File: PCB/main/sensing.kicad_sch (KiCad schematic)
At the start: 2 parts

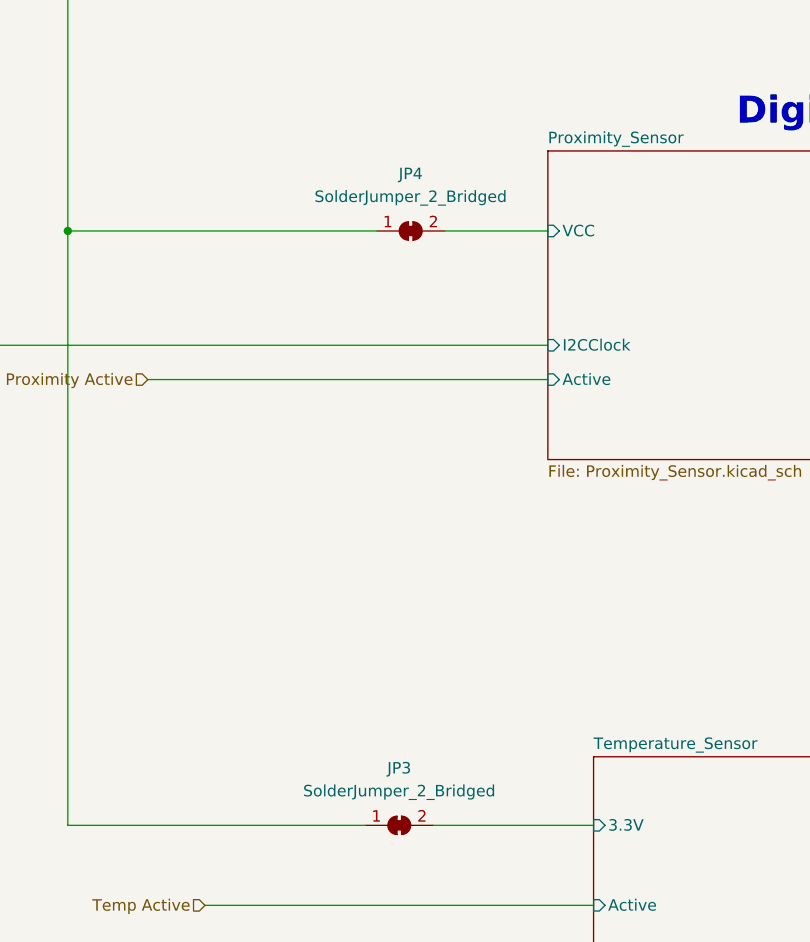
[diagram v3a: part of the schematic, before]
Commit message: Add footprints
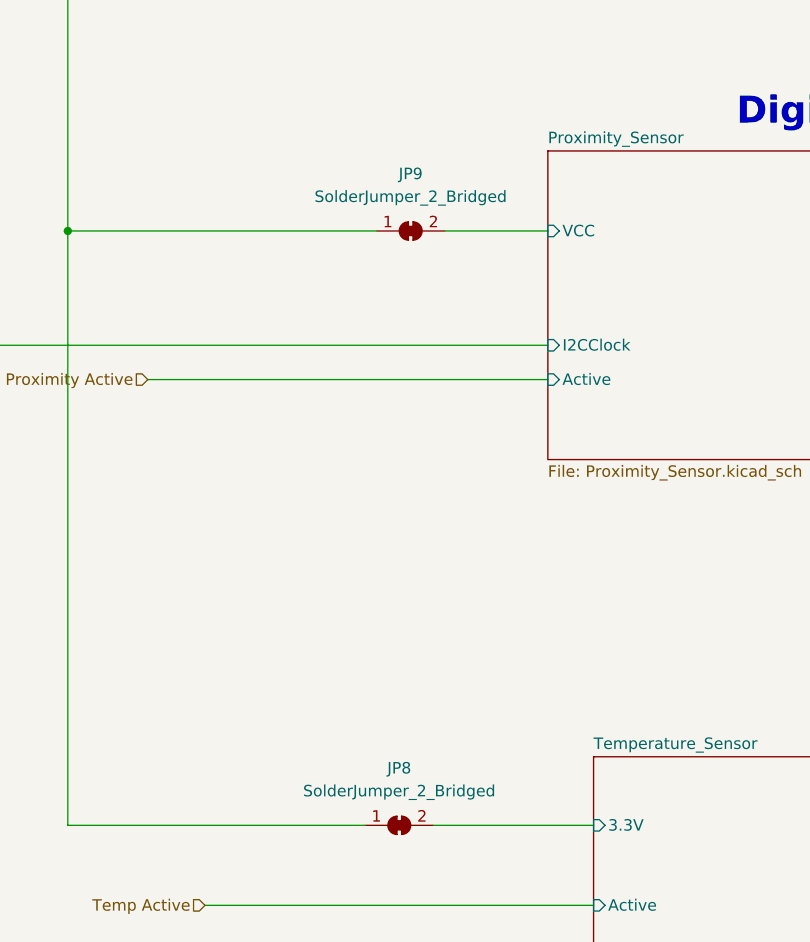
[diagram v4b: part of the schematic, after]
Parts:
- renumbered JP3 to JP8, JP4 to JP9
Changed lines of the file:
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@@
   (symbol (lib_id "Jumper:SolderJumper_2_Bridged") (at 234.95 92.71 0) (unit 1)
     (in_bom yes) (on_board yes) (fields_autoplaced)
-    (property "Reference" "JP4" (id 0) (at 234.95 86.36 0))
+    (property "Reference" "JP9" (id 0) (at 234.95 86.36 0))
     (property "Value" "SolderJumper_2_Bridged" (id 1) (at 234.95 88.9 0))
     (property "Footprint" "Jumper:SolderJumper-2_P1.3mm_Bridged2Bar_Pad1.0x1.5mm" (id 2) (at 234.95 92.71 0)
@@
   (symbol (lib_id "Jumper:SolderJumper_2_Bridged") (at 233.68 158.75 0) (unit 1)
     (in_bom yes) (on_board yes) (fields_autoplaced)
-    (property "Reference" "JP3" (id 0) (at 233.68 152.4 0))
+    (property "Reference" "JP8" (id 0) (at 233.68 152.4 0))
     (property "Value" "SolderJumper_2_Bridged" (id 1) (at 233.68 154.94 0))
     (property "Footprint" "Jumper:SolderJumper-2_P1.3mm_Bridged2Bar_Pad1.0x1.5mm" (id 2) (at 233.68 158.75 0)

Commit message: Design PCB
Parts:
- renumbered JP8 to JP5, JP9 to JP6
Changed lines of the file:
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@@
   (symbol (lib_id "Jumper:SolderJumper_2_Bridged") (at 234.95 92.71 0) (unit 1)
     (in_bom yes) (on_board yes) (fields_autoplaced)
-    (property "Reference" "JP9" (id 0) (at 234.95 86.36 0))
+    (property "Reference" "JP6" (id 0) (at 234.95 86.36 0))
     (property "Value" "SolderJumper_2_Bridged" (id 1) (at 234.95 88.9 0))
     (property "Footprint" "Jumper:SolderJumper-2_P1.3mm_Bridged2Bar_Pad1.0x1.5mm" (id 2) (at 234.95 92.71 0)
@@
   (symbol (lib_id "Jumper:SolderJumper_2_Bridged") (at 233.68 158.75 0) (unit 1)
     (in_bom yes) (on_board yes) (fields_autoplaced)
-    (property "Reference" "JP8" (id 0) (at 233.68 152.4 0))
+    (property "Reference" "JP5" (id 0) (at 233.68 152.4 0))
     (property "Value" "SolderJumper_2_Bridged" (id 1) (at 233.68 154.94 0))
     (property "Footprint" "Jumper:SolderJumper-2_P1.3mm_Bridged2Bar_Pad1.0x1.5mm" (id 2) (at 233.68 158.75 0)
